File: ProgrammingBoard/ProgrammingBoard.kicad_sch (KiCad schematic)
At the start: 0 parts

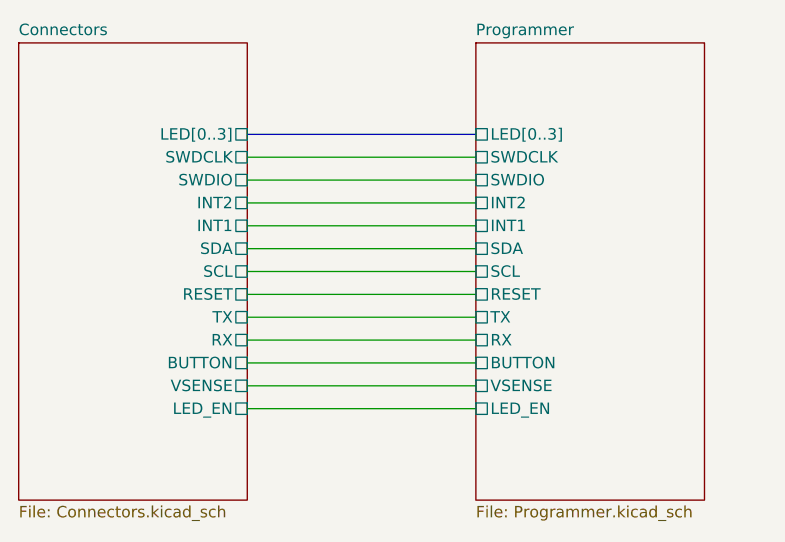
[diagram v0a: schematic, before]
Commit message: Remove LED driver
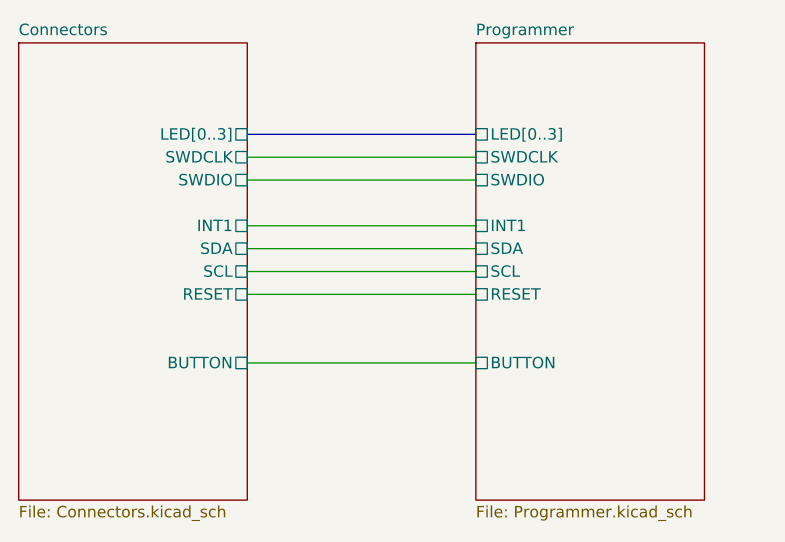
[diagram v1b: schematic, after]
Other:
- sheet Connectors ports: added none; removed INT2, LED_EN, RX, TX, VSENSE
- sheet Programmer ports: added none; removed INT2, LED_EN, RX, TX, VSENSE
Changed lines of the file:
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@@
-    (stroke (width 0) (type default))
-  )
-  (wire (pts (xy 88.9 81.28) (xy 114.3 81.28))
     (stroke (width 0) (type default))
   )
@@
     (stroke (width 0) (type default))
   )
-  (wire (pts (xy 88.9 104.14) (xy 114.3 104.14))
-    (stroke (width 0) (type default))
-  )
-  (wire (pts (xy 88.9 96.52) (xy 114.3 96.52))
-    (stroke (width 0) (type default))
-  )
   (wire (pts (xy 88.9 91.44) (xy 114.3 91.44))
-    (stroke (width 0) (type default))
-  )
-  (wire (pts (xy 88.9 93.98) (xy 114.3 93.98))
     (stroke (width 0) (type default))
   )
@@
   )
   (wire (pts (xy 88.9 83.82) (xy 114.3 83.82))
-    (stroke (width 0) (type default))
-  )
-  (wire (pts (xy 88.9 101.6) (xy 114.3 101.6))
     (stroke (width 0) (type default))
   )
@@
       (effects (font (size 1.27 1.27)) (justify right))
     )
-    (pin "INT2" passive (at 88.9 81.28 0)
-      (effects (font (size 1.27 1.27)) (justify right))
-    )
     (pin "RESET" passive (at 88.9 91.44 0)
       (effects (font (size 1.27 1.27)) (justify right))
@@
       (effects (font (size 1.27 1.27)) (justify right))
     )
-    (pin "TX" passive (at 88.9 93.98 0)
-      (effects (font (size 1.27 1.27)) (justify right))
-    )
-    (pin "RX" passive (at 88.9 96.52 0)
-      (effects (font (size 1.27 1.27)) (justify right))
-    )
     (pin "BUTTON" passive (at 88.9 99.06 0)
       (effects (font (size 1.27 1.27)) (justify right))
     )
     (pin "SCL" passive (at 88.9 88.9 0)
-      (effects (font (size 1.27 1.27)) (justify right))
-    )
-    (pin "VSENSE" passive (at 88.9 101.6 0)
-      (effects (font (size 1.27 1.27)) (justify right))
-    )
-    (pin "LED_EN" passive (at 88.9 104.14 0)
       (effects (font (size 1.27 1.27)) (justify right))
     )
@@
       (effects (font (size 1.27 1.27)) (justify left))
     )
-    (pin "INT2" passive (at 114.3 81.28 180)
-      (effects (font (size 1.27 1.27)) (justify left))
-    )
     (pin "SWDCLK" passive (at 114.3 76.2 180)
-      (effects (font (size 1.27 1.27)) (justify left))
-    )
-    (pin "RX" passive (at 114.3 96.52 180)
-      (effects (font (size 1.27 1.27)) (justify left))
-    )
-    (pin "VSENSE" passive (at 114.3 101.6 180)
-      (effects (font (size 1.27 1.27)) (justify left))
-    )
-    (pin "TX" passive (at 114.3 93.98 180)
       (effects (font (size 1.27 1.27)) (justify left))
     )
@@
       (effects (font (size 1.27 1.27)) (justify left))
     )
-    (pin "LED_EN" passive (at 114.3 104.14 180)
-      (effects (font (size 1.27 1.27)) (justify left))
-    )

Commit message: Change led matrix routing for sinking current through mcu, sourcing from battery
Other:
- title: (none) -> WordWatch - Programming Board
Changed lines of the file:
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@@
 (kicad_sch (version 20230121) (generator eeschema)
   (paper "A4")
+  (title_block
+    (title "WordWatch - Programming Board")
+    (date "2023-11-11")
+    (rev "1.0")
+  )
   (wire (pts (xy 88.9 88.9) (xy 114.3 88.9))
     (stroke (width 0) (type default))
